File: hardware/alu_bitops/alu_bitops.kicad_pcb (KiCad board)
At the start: 4 copper layers, 99 x 99 mm, 230 parts, among them J1 Conn_02x21_Odd_Even, Q1 IRLML6244, Q10 IRLML6244, Q11 IRLML6244, Q12 IRLML6244, Q13 IRLML6244, Q14 IRLML6244, Q15 IRLML6244, Q16 IRLML6244, Q17 IRLML6244, Q18 IRLML6244, Q19 IRLML6244, Q2 IRLML6244, Q20 IRLML6244, Q21 IRLML6244, Q22 IRLML6244, Q23 IRLML6244, Q24 IRLML6244, Q25 IRLML6244, Q26 IRLML6244, Q27 IRLML6244, Q28 IRLML6244, Q29 IRLML6244, Q3 IRLML6244, Q30 IRLML6244, Q4 IRLML6244, Q5 IRLML6244, Q6 IRLML6244, Q7 IRLML6244, Q8 IRLML6244, Q9 IRLML6244, U1 74HC00, U10 74HC00, U11 74HC00, U12 74HC00, U13 74HC00, U14 74HC00, U15 74HC00, U16 74HC00, U17 74HC00, U18 74HC00, U19 74HC00, U2 74HC00, U20 74HC00, U21 74HC00, U22 74HC00, U23 74HC00, U24 74HC00, U25 74HC00, U26 74HC00, U27 74HC00, U28 74HC00, U29 74HC00, U3 74HC00, U30 74HC00, U31 74HC00, U32 74HC00, U33 74HC00, U34 74HC00, U35 74HC00, U4 74HC00, U5 74HC00, U6 74HC00, U7 74HC00, U8 74HC00, U9 74HC00

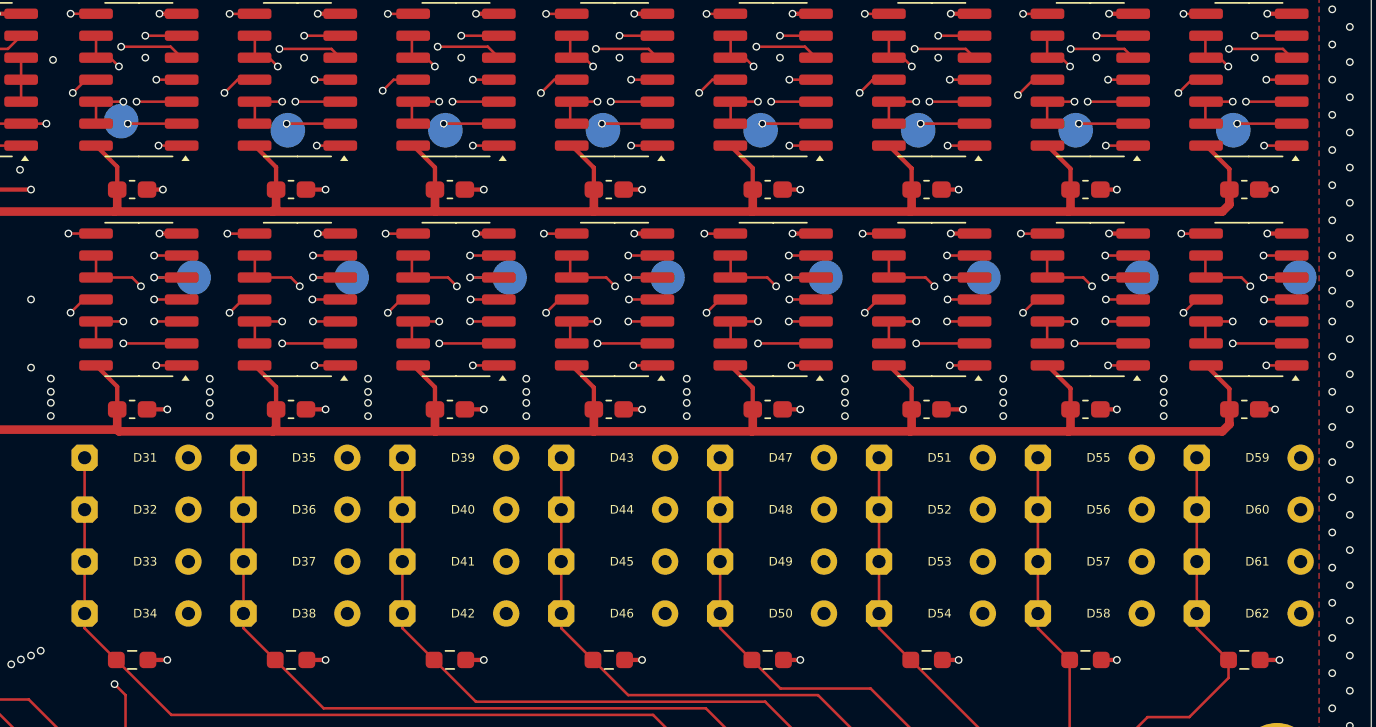
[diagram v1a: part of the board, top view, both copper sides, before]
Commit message: ALU shifter, bitops and motherboard as ordered
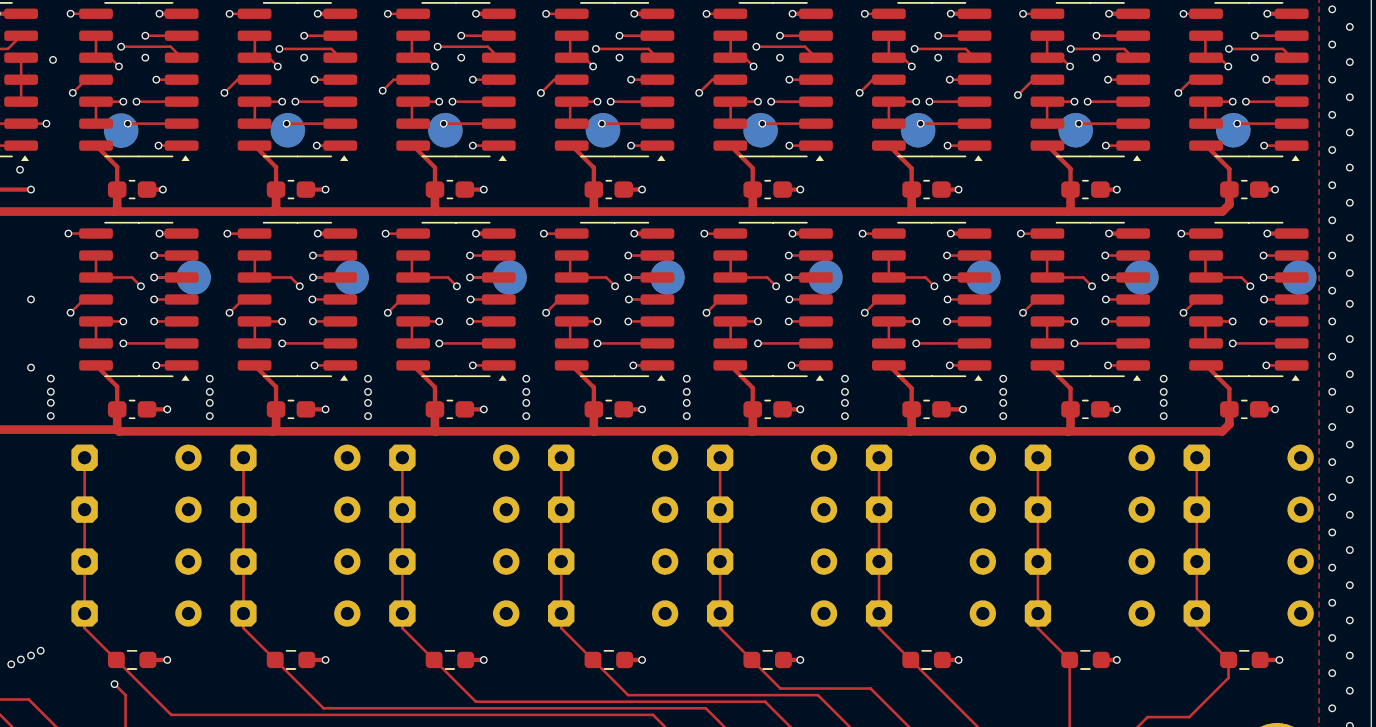
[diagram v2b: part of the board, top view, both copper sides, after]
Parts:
- moved TP1 0.54 mm to (71.2, 102.0)
